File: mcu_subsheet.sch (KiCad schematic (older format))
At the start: 5 parts

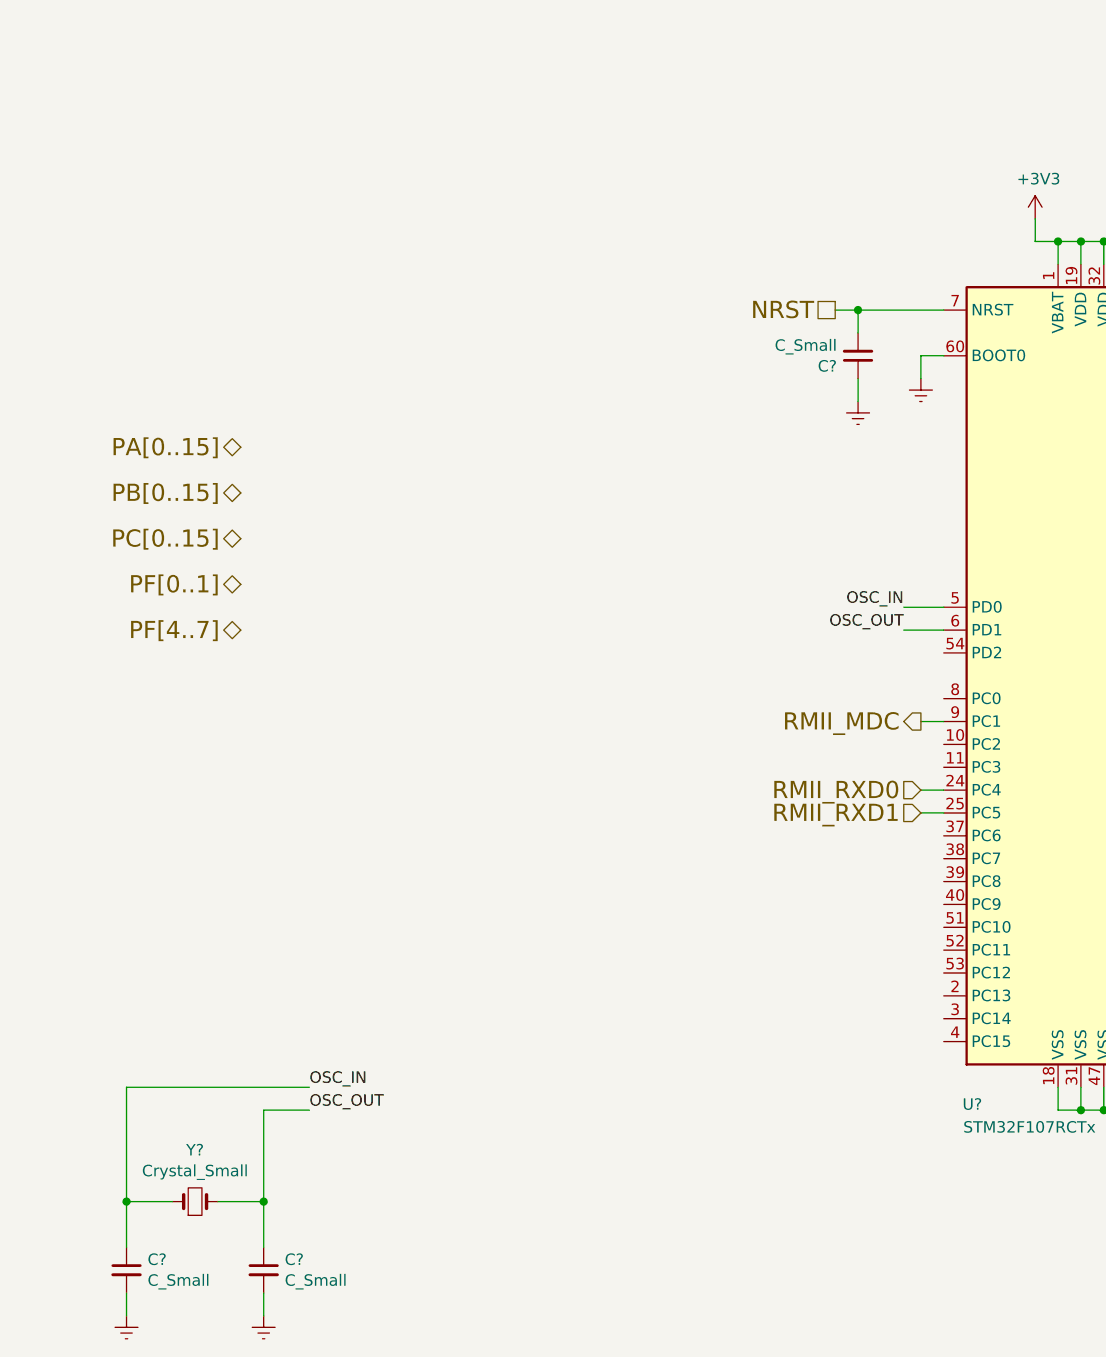
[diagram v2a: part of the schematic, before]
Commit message: [Cangate]: mcu leds and osc added
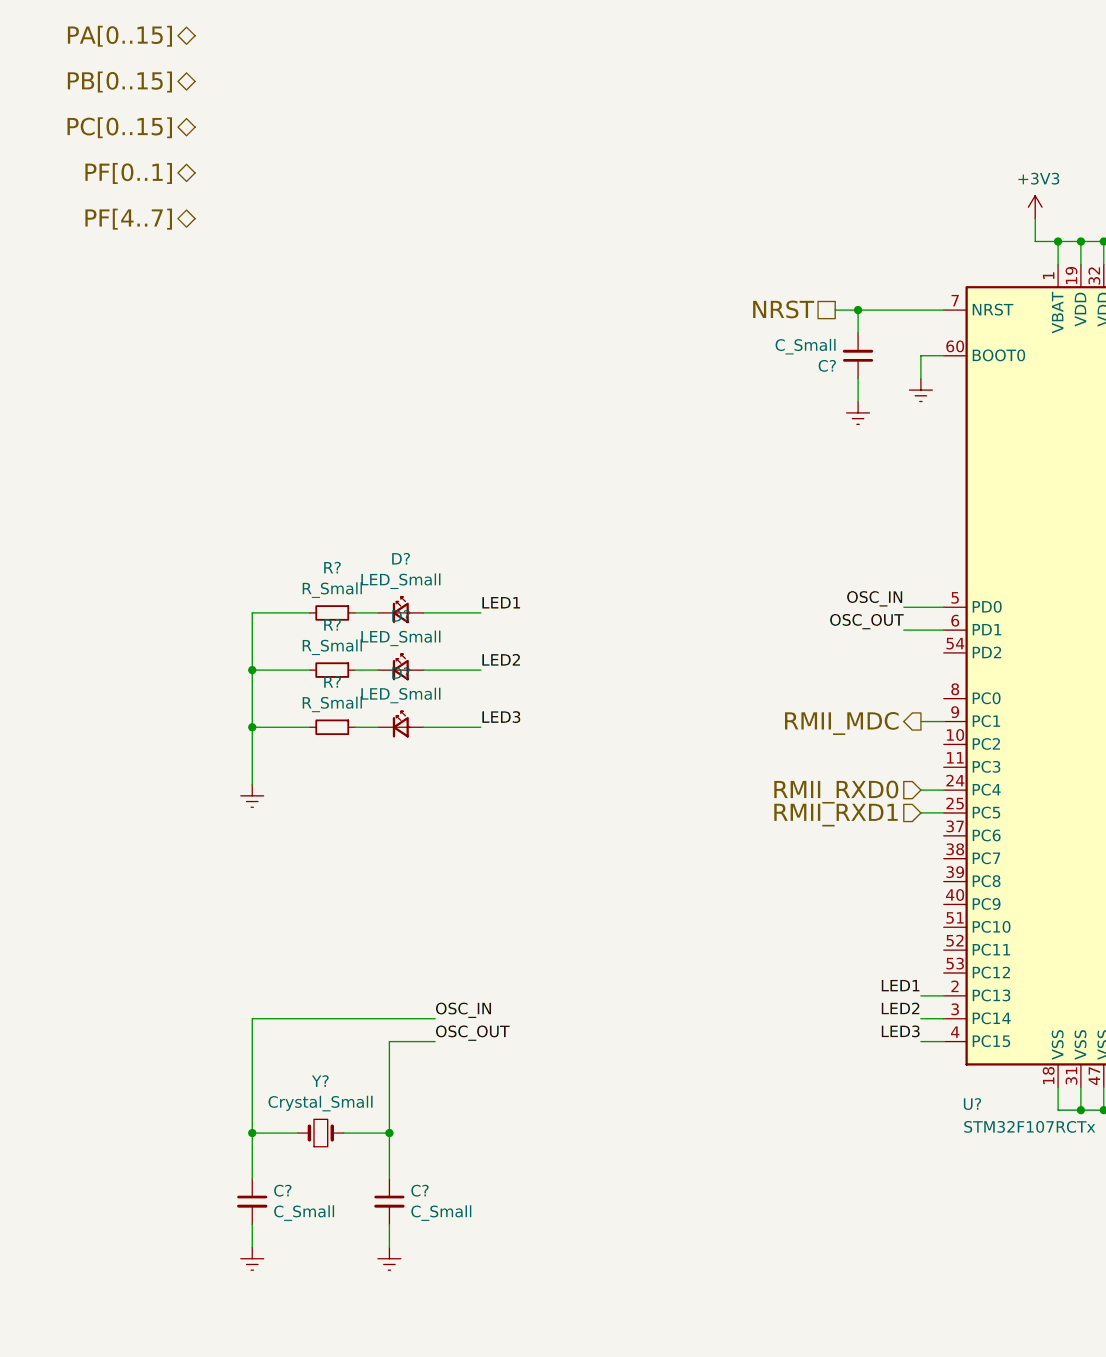
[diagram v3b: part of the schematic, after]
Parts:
- added D? (x3): LED_Small, symbol Device:LED_Small
- added R? (x3): R_Small, symbol Device:R_Small
- Y?: footprint Crystal:Crystal_SMD_Abracon_ABM3-2Pin_5.0x3.2mm_HandSoldering -> Crystal:Crystal_SMD_Abracon_ABM3B-4Pin_5.0x3.2mm
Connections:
- net Earth: now also R?.2, R?.2, R?.2
- net LED1: now reaches U?.2 (PC13)
- net LED1: now also D?.2 (A)
- net LED2: now reaches U?.3 (PC14)
- net LED2: now also D?.2 (A)
- net LED3: now reaches U?.4 (PC15)
- net LED3: now also D?.2 (A)
- new net: D?.1 (K), R?.1 (x3)
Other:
- moved on the sheet: C?, Y?
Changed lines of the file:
@@
 Text HLabel 4300 2400 0    75   UnSpc ~ 0
 NRST
-Text HLabel 1700 3000 0    75   BiDi ~ 0
+Text HLabel 1500 1200 0    75   BiDi ~ 0
 PA[0..15]
-Text HLabel 1700 3200 0    75   BiDi ~ 0
+Text HLabel 1500 1400 0    75   BiDi ~ 0
 PB[0..15]
-Text HLabel 1700 3400 0    75   BiDi ~ 0
+Text HLabel 1500 1600 0    75   BiDi ~ 0
 PC[0..15]
-Text HLabel 1700 3600 0    75   BiDi ~ 0
+Text HLabel 1500 1800 0    75   BiDi ~ 0
 PF[0..1]
-Text HLabel 1700 3800 0    75   BiDi ~ 0
+Text HLabel 1500 2000 0    75   BiDi ~ 0
 PF[4..7]
 Wire Wire Line
@@
 L Device:Crystal_Small Y?
 U 1 1 61D4BE60
-P 1500 6300
+P 2050 6000
 AR Path="/6176B826/61D4BE60" Ref="Y?"  Part="1"
 AR Path="/6176B761/61D4BE60" Ref="Y?"  Part="1"
-F 0 "Y?" H 1500 6525 50  0000 C CNN
-F 1 "Crystal_Small" H 1500 6434 50  0000 C CNN
-F 2 "Crystal:Crystal_SMD_Abracon_ABM3-2Pin_5.0x3.2mm_HandSoldering" H 1500 6300 50  0001 C CNN
-F 3 "~" H 1500 6300 50  0001 C CNN
-	1    1500 6300
+F 0 "Y?" H 2050 6225 50  0000 C CNN
+F 1 "Crystal_Small" H 2050 6134 50  0000 C CNN
+F 2 "Crystal:Crystal_SMD_Abracon_ABM3B-4Pin_5.0x3.2mm" H 2050 6000 50  0001 C CNN
+F 3 "~" H 2050 6000 50  0001 C CNN
+	1    2050 6000
 	1    0    0    -1
 $EndComp
@@
 L Device:C_Small C?
 U 1 1 61D4BE67
-P 1200 6600
+P 1750 6300
 AR Path="/6176B826/61D4BE67" Ref="C?"  Part="1"
 AR Path="/6176B761/61D4BE67" Ref="C?"  Part="1"
-F 0 "C?" H 1292 6646 50  0000 L CNN
-F 1 "C_Small" H 1292 6555 50  0000 L CNN
-F 2 "" H 1200 6600 50  0001 C CNN
-F 3 "~" H 1200 6600 50  0001 C CNN
-	1    1200 6600
+F 0 "C?" H 1842 6346 50  0000 L CNN
+F 1 "C_Small" H 1842 6255 50  0000 L CNN
+F 2 "" H 1750 6300 50  0001 C CNN
+F 3 "~" H 1750 6300 50  0001 C CNN
+	1    1750 6300
 	1    0    0    -1
 $EndComp
@@
 L Device:C_Small C?
 U 1 1 61D4BE6D
-P 1800 6600
+P 2350 6300
 AR Path="/6176B826/61D4BE6D" Ref="C?"  Part="1"
 AR Path="/6176B761/61D4BE6D" Ref="C?"  Part="1"
-F 0 "C?" H 1892 6646 50  0000 L CNN
-F 1 "C_Small" H 1892 6555 50  0000 L CNN
-F 2 "" H 1800 6600 50  0001 C CNN
-F 3 "~" H 1800 6600 50  0001 C CNN
-	1    1800 6600
+F 0 "C?" H 2442 6346 50  0000 L CNN
+F 1 "C_Small" H 2442 6255 50  0000 L CNN
+F 2 "" H 2350 6300 50  0001 C CNN
+F 3 "~" H 2350 6300 50  0001 C CNN
+	1    2350 6300
 	1    0    0    -1
 $EndComp
@@
 L power:Earth #PWR?
 U 1 1 61D4BE73
-P 1200 6800
+P 1750 6500
 AR Path="/6176B826/61D4BE73" Ref="#PWR?"  Part="1"
 AR Path="/6176B761/61D4BE73" Ref="#PWR?"  Part="1"
-F 0 "#PWR?" H 1200 6550 50  0001 C CNN
-F 1 "Earth" H 1200 6650 50  0001 C CNN
-F 2 "" H 1200 6800 50  0001 C CNN
-F 3 "~" H 1200 6800 50  0001 C CNN
-	1    1200 6800
+F 0 "#PWR?" H 1750 6250 50  0001 C CNN
+F 1 "Earth" H 1750 6350 50  0001 C CNN
+F 2 "" H 1750 6500 50  0001 C CNN
+F 3 "~" H 1750 6500 50  0001 C CNN
+	1    1750 6500
 	1    0    0    -1
 $EndComp
@@
 L power:Earth #PWR?
 U 1 1 61D4BE79
-P 1800 6800
+P 2350 6500
 AR Path="/6176B826/61D4BE79" Ref="#PWR?"  Part="1"
 AR Path="/6176B761/61D4BE79" Ref="#PWR?"  Part="1"
-F 0 "#PWR?" H 1800 6550 50  0001 C CNN
-F 1 "Earth" H 1800 6650 50  0001 C CNN
-F 2 "" H 1800 6800 50  0001 C CNN
-F 3 "~" H 1800 6800 50  0001 C CNN
-	1    1800 6800
-	1    0    0    -1
-$EndComp
-Wire Wire Line
-	1200 6700 1200 6800
-Wire Wire Line
-	1800 6700 1800 6800
-Wire Wire Line
-	1400 6300 1200 6300
-Wire Wire Line
-	1200 6300 1200 6500
-Wire Wire Line
-	1600 6300 1800 6300
-Wire Wire Line
-	1800 6300 1800 6500
-Wire Wire Line
-	1200 6300 1200 5800
-Wire Wire Line
-	1200 5800 2000 5800
-Connection ~ 1200 6300
-Wire Wire Line
-	1800 6300 1800 5900
-Wire Wire Line
-	1800 5900 2000 5900
-Connection ~ 1800 6300
-Text Label 2000 5800 0    50   ~ 0
+F 0 "#PWR?" H 2350 6250 50  0001 C CNN
+F 1 "Earth" H 2350 6350 50  0001 C CNN
+F 2 "" H 2350 6500 50  0001 C CNN
+F 3 "~" H 2350 6500 50  0001 C CNN
+	1    2350 6500
+	1    0    0    -1
+$EndComp
+Wire Wire Line
+	1750 6400 1750 6500
+Wire Wire Line
+	2350 6400 2350 6500
+Wire Wire Line
+	1950 6000 1750 6000
+Wire Wire Line
+	1750 6000 1750 6200
+Wire Wire Line
+	2150 6000 2350 6000
+Wire Wire Line
+	2350 6000 2350 6200
+Wire Wire Line
+	1750 6000 1750 5500
+Wire Wire Line
+	1750 5500 2550 5500
+Connection ~ 1750 6000
+Wire Wire Line
+	2350 6000 2350 5600
+Wire Wire Line
+	2350 5600 2550 5600
+Connection ~ 2350 6000
+Text Label 2550 5500 0    50   ~ 0
 OSC_IN
 Text Label 4600 3700 2    50   ~ 0
@@
 Text Label 4600 3800 2    50   ~ 0
 OSC_OUT
-Text Label 2000 5900 0    50   ~ 0
+Text Label 2550 5600 0    50   ~ 0
 OSC_OUT
+Wire Wire Line
+	4775 5400 4675 5400
+Wire Wire Line
+	4775 5500 4675 5500
+Wire Wire Line
+	4775 5600 4675 5600
+Text Label 4675 5400 2    50   ~ 0
+LED1
+Text Label 4675 5500 2    50   ~ 0
+LED2
+Text Label 4675 5600 2    50   ~ 0
+LED3
+Text Label 2750 3725 0    50   ~ 0
+LED1
+Text Label 2750 3975 0    50   ~ 0
+LED2
+Text Label 2750 4225 0    50   ~ 0
+LED3
+$Comp
+L power:Earth #PWR?
+U 1 1 61D4FCF2
+P 1750 4475
+F 0 "#PWR?" H 1750 4225 50  0001 C CNN
+F 1 "Earth" H 1750 4325 50  0001 C CNN
+F 2 "" H 1750 4475 50  0001 C CNN
+F 3 "~" H 1750 4475 50  0001 C CNN
+	1    1750 4475
+	1    0    0    -1
+$EndComp
+$Comp
+L Device:LED_Small D?
+U 1 1 61D516FC
+P 2400 3725
+F 0 "D?" H 2400 3960 50  0000 C CNN
+F 1 "LED_Small" H 2400 3869 50  0000 C CNN
+F 2 "" V 2400 3725 50  0001 C CNN
+F 3 "~" V 2400 3725 50  0001 C CNN
+	1    2400 3725
+	1    0    0    -1
+$EndComp
+$Comp
+L Device:LED_Small D?
+U 1 1 61D52243
+P 2400 3975
+F 0 "D?" H 2400 4210 50  0000 C CNN
+F 1 "LED_Small" H 2400 4119 50  0000 C CNN
+F 2 "" V 2400 3975 50  0001 C CNN
+F 3 "~" V 2400 3975 50  0001 C CNN
+	1    2400 3975
+	1    0    0    -1
+$EndComp
+$Comp
+L Device:LED_Small D?
+U 1 1 61D525E2
+P 2400 4225
+F 0 "D?" H 2400 4460 50  0000 C CNN
+F 1 "LED_Small" H 2400 4369 50  0000 C CNN
+F 2 "" V 2400 4225 50  0001 C CNN
+F 3 "~" V 2400 4225 50  0001 C CNN
+	1    2400 4225
+	1    0    0    -1
+$EndComp
+Wire Wire Line
+	2500 4225 2750 4225
+Wire Wire Line
+	2500 3975 2750 3975
+Wire Wire Line
+	2500 3725 2750 3725
+$Comp
+L Device:R_Small R?
+U 1 1 61D57F68
+P 2100 3725
+F 0 "R?" V 1904 3725 50  0000 C CNN
+F 1 "R_Small" V 1995 3725 50  0000 C CNN
+F 2 "" H 2100 3725 50  0001 C CNN
+F 3 "~" H 2100 3725 50  0001 C CNN
+	1    2100 3725
+	0    1    1    0
+$EndComp
+Wire Wire Line
+	2200 3725 2300 3725
+$Comp
+L Device:R_Small R?
+U 1 1 61D59E4A
+P 2100 3975
+F 0 "R?" V 1904 3975 50  0000 C CNN
+F 1 "R_Small" V 1995 3975 50  0000 C CNN
+F 2 "" H 2100 3975 50  0001 C CNN
+F 3 "~" H 2100 3975 50  0001 C CNN
+	1    2100 3975
+	0    1    1    0
+$EndComp
+$Comp
+L Device:R_Small R?
+U 1 1 61D5A67A
+P 2100 4225
+F 0 "R?" V 1904 4225 50  0000 C CNN
+F 1 "R_Small" V 1995 4225 50  0000 C CNN
+F 2 "" H 2100 4225 50  0001 C CNN
+F 3 "~" H 2100 4225 50  0001 C CNN
+	1    2100 4225
+	0    1    1    0
+$EndComp
+Wire Wire Line
+	2200 4225 2300 4225
+Wire Wire Line
+	2200 3975 2300 3975
+Wire Wire Line
+	1750 4475 1750 4225
+Wire Wire Line
+	1750 4225 2000 4225
+Wire Wire Line
+	2000 3725 1750 3725
+Wire Wire Line
+	1750 3725 1750 3975
+Connection ~ 1750 4225
+Wire Wire Line
+	2000 3975 1750 3975
+Connection ~ 1750 3975
+Wire Wire Line
+	1750 3975 1750 4225
 $EndSCHEMATC

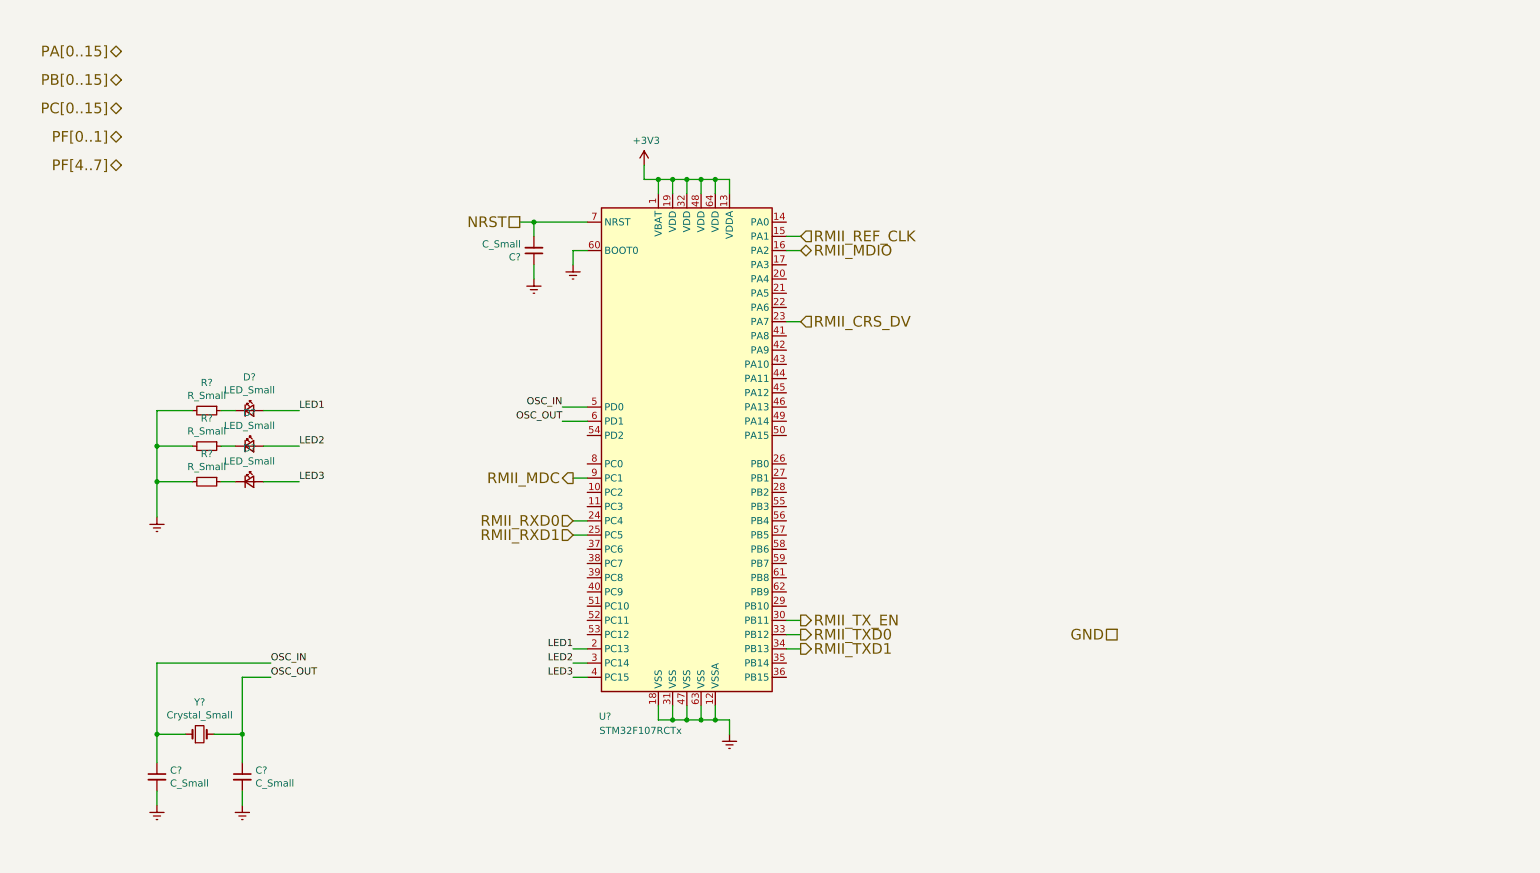
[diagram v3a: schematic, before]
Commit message: [Cangate]: end with base schematics.
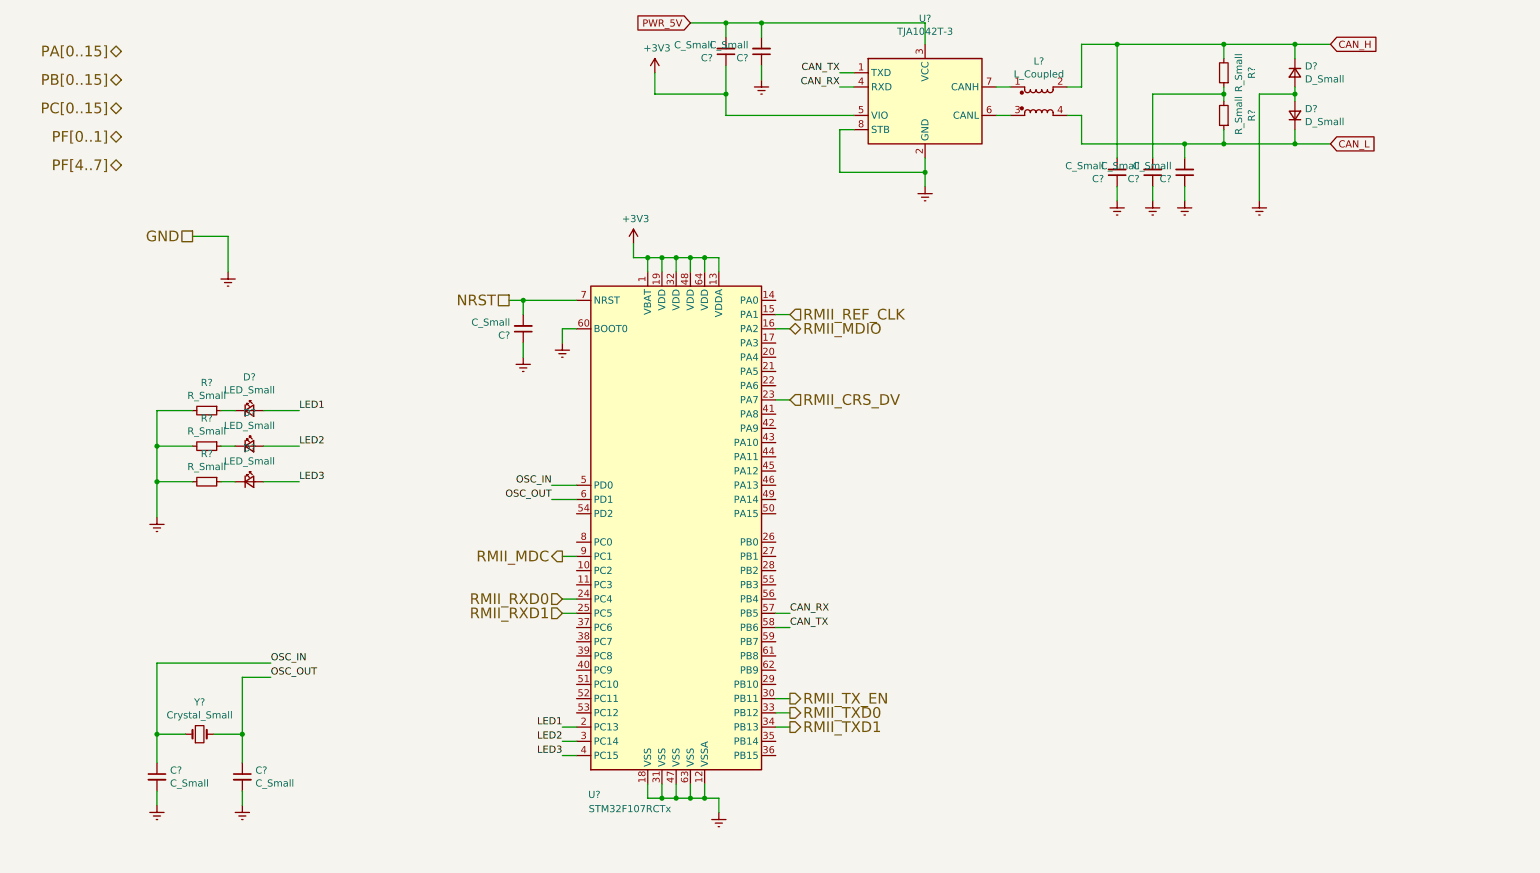
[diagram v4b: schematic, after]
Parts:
- added C? (x5): C_Small, symbol Device:C_Small
- added D? (x2): D_Small, symbol Device:D_Small
- added L?: L_Coupled, Inductor_SMD:L_CommonModeChoke_Coilcraft_1812CAN, symbol Device:L_Coupled
- added R? (x2): R_Small, symbol Device:R_Small
- added U?: TJA1042T-3, Package_SO:SOIC-8_3.9x4.9mm_P1.27mm, symbol Interface_CAN_LIN:TJA1042T-3
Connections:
- net +3V3: now also C?.1, U?.5 (VIO)
- net Earth: now also C?.1, C?.1, C?.1, C?.1, D?.2 (A), D?.2 (A), U?.2 (GND), U?.8 (STB)
- net CAN_RX: now reaches U?.57 (PB5)
- net CAN_RX: now also U?.4 (RXD)
- net CAN_TX: now reaches U?.58 (PB6)
- net CAN_TX: now also U?.1 (TXD)
- new net: L?.3, U?.6 (CANL)
- new net: L?.1, U?.7 (CANH)
- new net: C?.2, R?.1, R?.2
- new net CAN_H: C?.2, D?.1 (K), L?.2, R?.2
- new net CAN_L: C?.2, D?.1 (K), L?.4, R?.1
- new net PWR_5V: C?.2, C?.2, U?.3 (VCC)
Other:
- moved on the sheet: C?, U?
